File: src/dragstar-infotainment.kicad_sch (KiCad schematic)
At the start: 0 parts

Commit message: update Schematics
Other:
- note removed: "Labels are in reference to the local I/O scope boxes Labels at the cable harness are in reference to the Bus I/O Wire gauge: 1mm² / 18AWG"
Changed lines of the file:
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@@
     (date "2023-04-12")
     (rev "2.4")
-  )
-  (text "Labels are in reference to the local I/O scope boxes\nLabels at the cable harness are in reference to the Bus I/O\n\nWire gauge: 1mm² / 18AWG"
-    (at 177.8 180.34 0)
-    (effects (font (size 1.27 1.27)) (justify left bottom))
+    (comment 1 "Wire gauge: 1mm² / 18AWG")
+    (comment 3 "Labels at the cable harness are in reference to each connected component")
+    (comment 4 "Labels are in reference to the local I/O scope boxes")
   )
   (sheet (at 203.2 88.9) (size 76.2 50.8) (fields_autoplaced)

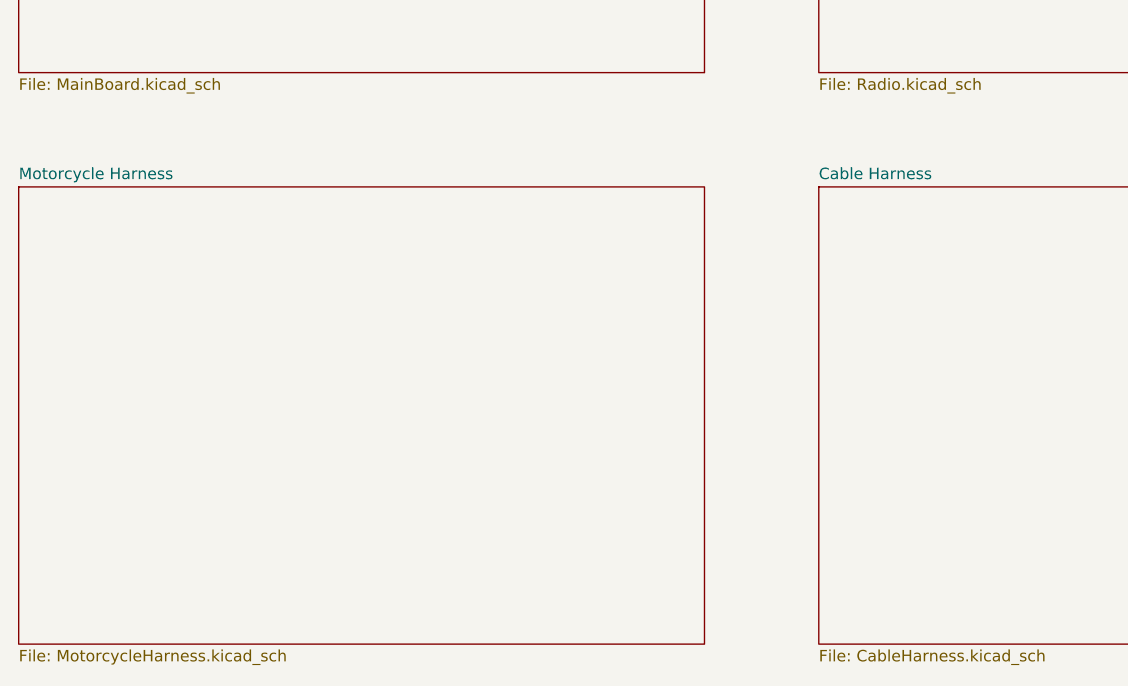
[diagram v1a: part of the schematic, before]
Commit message: simplify circuit diagram. Remove unecessary features; Split board into two components|
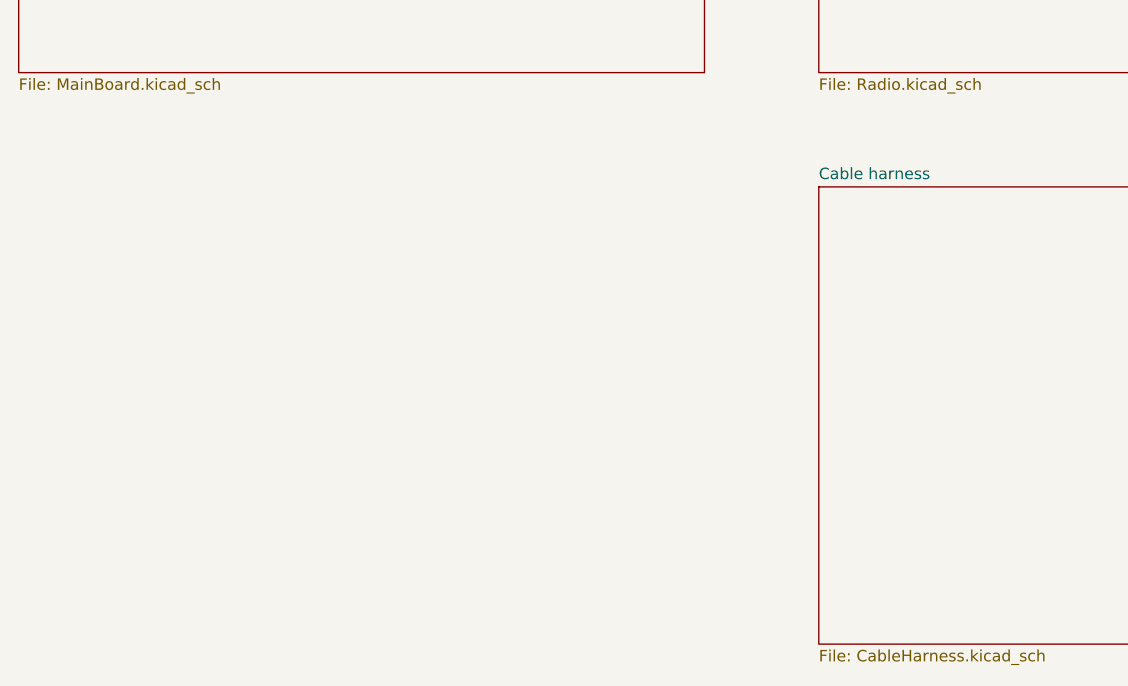
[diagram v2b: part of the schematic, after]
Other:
- sheet Cable Harness renamed Cable harness
- removed sheet Motorcycle Harness
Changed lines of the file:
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@@
     (date "2023-04-12")
     (rev "2.4")
-    (comment 1 "Wire gauge: 1mm² / 18AWG")
-    (comment 3 "Labels at the cable harness are in reference to each connected component")
-    (comment 4 "Labels are in reference to the local I/O scope boxes")
+    (comment 4 "Wire gauge: 1mm² / 18AWG")
   )
   (sheet (at 203.2 88.9) (size 76.2 50.8) (fields_autoplaced)
@@
     (stroke (width 0.1524) (type solid))
     (fill (color 0 0 0 0.0000))
-    (property "Sheetname" "Cable Harness" (at 114.3 88.1884 0)
+    (property "Sheetname" "Cable harness" (at 114.3 88.1884 0)
       (effects (font (size 1.27 1.27)) (justify left bottom))
     )
@@
       )
     )
-  )
-  (sheet (at 25.4 88.9) (size 76.2 50.8) (fields_autoplaced)
-    (stroke (width 0.1524) (type solid))
-    (fill (color 0 0 0 0.0000))
-    (property "Sheetname" "Motorcycle Harness" (at 25.4 88.1884 0)
-      (effects (font (size 1.27 1.27)) (justify left bottom))
-    )
-    (property "Sheetfile" "MotorcycleHarness.kicad_sch" (at 25.4 140.2846 0)
-      (effects (font (size 1.27 1.27)) (justify left top))
-    )
-    (instances
-      (project "dragstar-infotainment"
-        (path "/e63e39d7-6ac0-4ffd-8aa3-1841a4541b55" (page "6"))
-      )
-    )

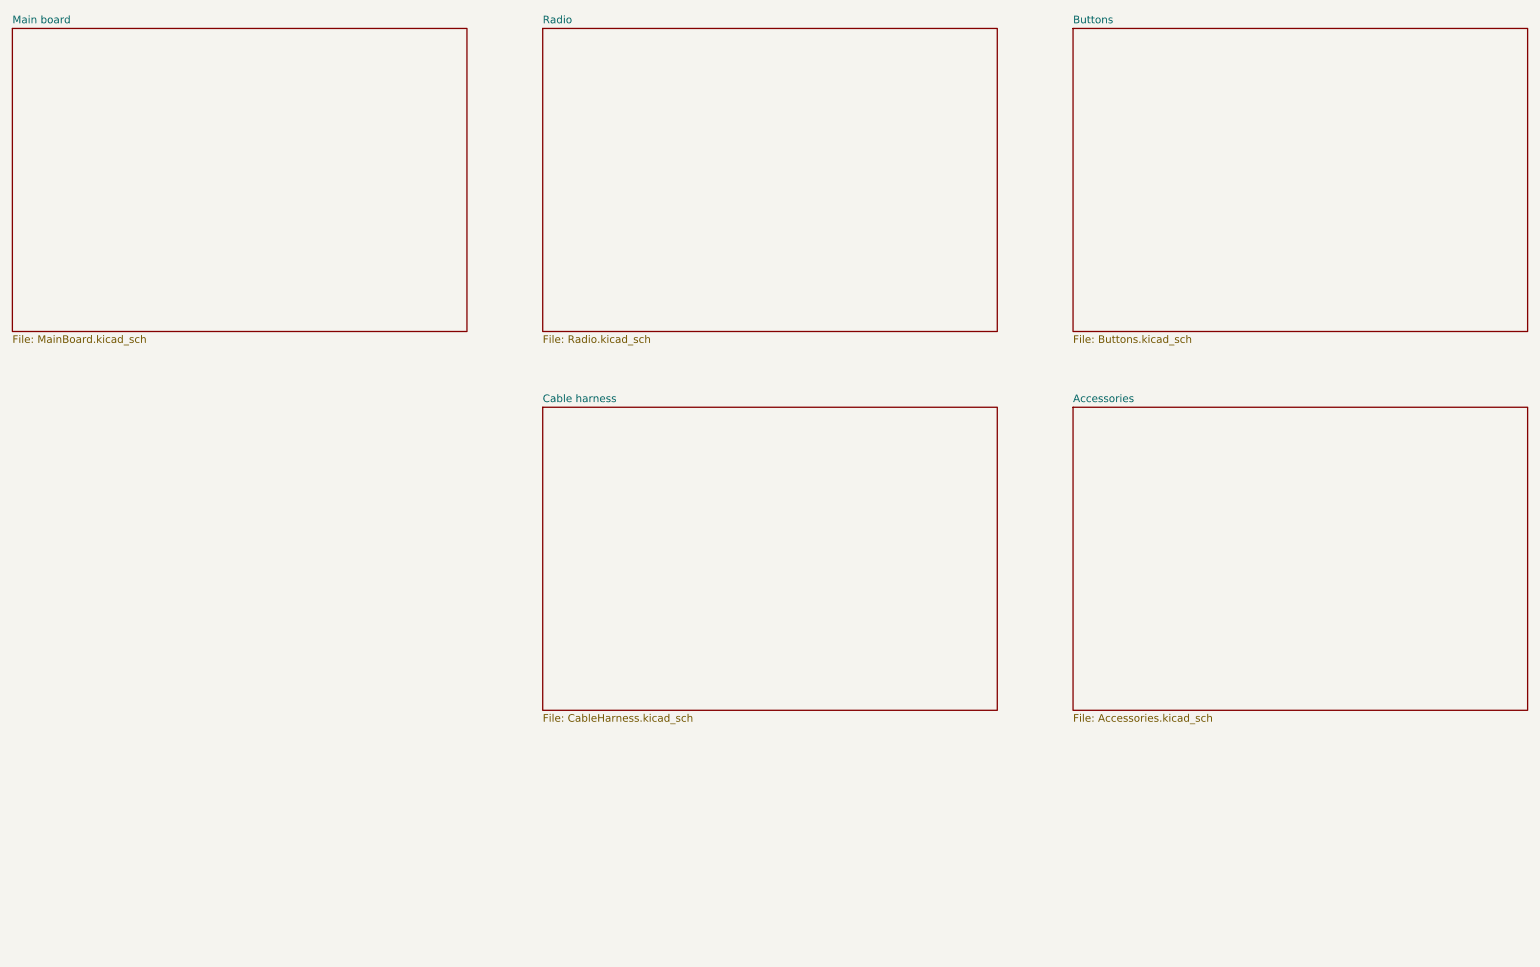
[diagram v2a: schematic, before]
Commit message: Simplify circuit diagram. Remove unecessary features
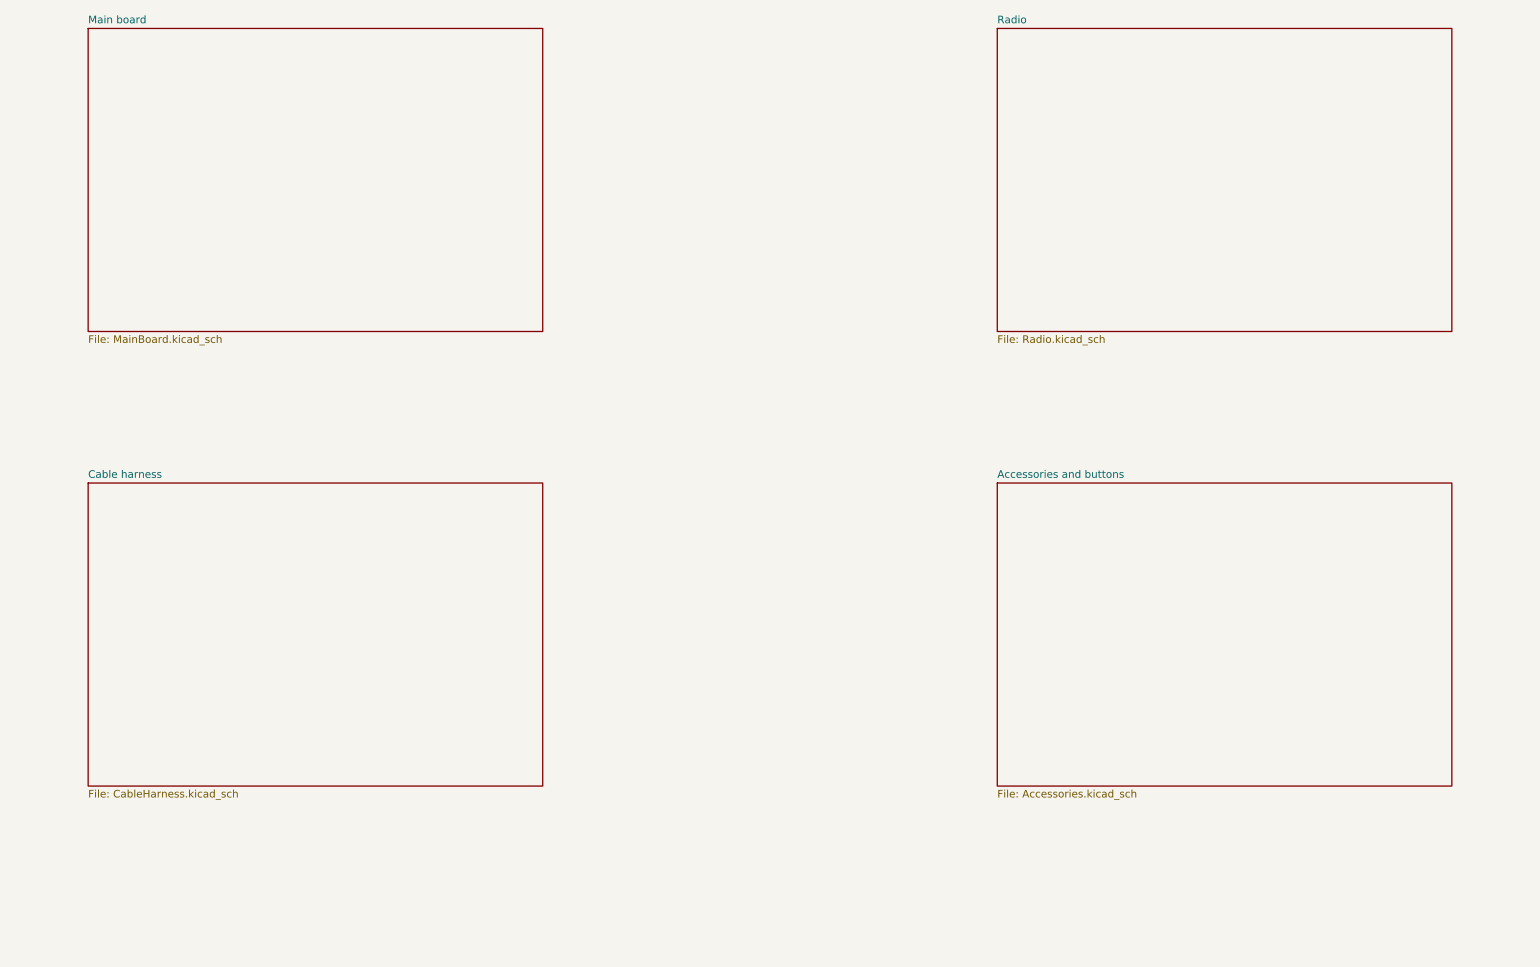
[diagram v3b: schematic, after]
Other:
- sheet Accessories renamed Accessories and buttons
- removed sheet Buttons
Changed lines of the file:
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@@
     (comment 4 "Wire gauge: 1mm² / 18AWG")
   )
-  (sheet (at 203.2 88.9) (size 76.2 50.8) (fields_autoplaced)
+  (sheet (at 190.5 101.6) (size 76.2 50.8) (fields_autoplaced)
     (stroke (width 0.1524) (type solid))
     (fill (color 0 0 0 0.0000))
-    (property "Sheetname" "Accessories" (at 203.2 88.1884 0)
+    (property "Sheetname" "Accessories and buttons" (at 190.5 100.8884 0)
       (effects (font (size 1.27 1.27)) (justify left bottom))
     )
-    (property "Sheetfile" "Accessories.kicad_sch" (at 203.2 140.2846 0)
+    (property "Sheetfile" "Accessories.kicad_sch" (at 190.5 152.9846 0)
       (effects (font (size 1.27 1.27)) (justify left top))
     )
@@
     )
   )
-  (sheet (at 25.4 25.4) (size 76.2 50.8) (fields_autoplaced)
+  (sheet (at 38.1 25.4) (size 76.2 50.8) (fields_autoplaced)
     (stroke (width 0.1524) (type solid))
     (fill (color 0 0 0 0.0000))
-    (property "Sheetname" "Main board" (at 25.4 24.6884 0)
+    (property "Sheetname" "Main board" (at 38.1 24.6884 0)
       (effects (font (size 1.27 1.27)) (justify left bottom))
     )
-    (property "Sheetfile" "MainBoard.kicad_sch" (at 25.4 76.7846 0)
+    (property "Sheetfile" "MainBoard.kicad_sch" (at 38.1 76.7846 0)
       (effects (font (size 1.27 1.27)) (justify left top))
     )
@@
     )
   )
-  (sheet (at 114.3 88.9) (size 76.2 50.8) (fields_autoplaced)
+  (sheet (at 38.1 101.6) (size 76.2 50.8) (fields_autoplaced)
     (stroke (width 0.1524) (type solid))
     (fill (color 0 0 0 0.0000))
-    (property "Sheetname" "Cable harness" (at 114.3 88.1884 0)
+    (property "Sheetname" "Cable harness" (at 38.1 100.8884 0)
       (effects (font (size 1.27 1.27)) (justify left bottom))
     )
-    (property "Sheetfile" "CableHarness.kicad_sch" (at 114.3 140.2846 0)
+    (property "Sheetfile" "CableHarness.kicad_sch" (at 38.1 152.9846 0)
       (effects (font (size 1.27 1.27)) (justify left top))
     )
@@
     )
   )
-  (sheet (at 203.2 25.4) (size 76.2 50.8) (fields_autoplaced)
+  (sheet (at 190.5 25.4) (size 76.2 50.8) (fields_autoplaced)
     (stroke (width 0.1524) (type solid))
     (fill (color 0 0 0 0.0000))
-    (property "Sheetname" "Buttons" (at 203.2 24.6884 0)
+    (property "Sheetname" "Radio" (at 190.5 24.6884 0)
       (effects (font (size 1.27 1.27)) (justify left bottom))
     )
-    (property "Sheetfile" "Buttons.kicad_sch" (at 203.2 76.7846 0)
+    (property "Sheetfile" "Radio.kicad_sch" (at 190.5 76.7846 0)
       (effects (font (size 1.27 1.27)) (justify left top))
     )
-    (instances
-      (project "dragstar-infotainment"
-        (path "/e63e39d7-6ac0-4ffd-8aa3-1841a4541b55" (page "3"))
-      )
-    )
-  )
-  (sheet (at 114.3 25.4) (size 76.2 50.8) (fields_autoplaced)
-    (stroke (width 0.1524) (type solid))
-    (fill (color 0 0 0 0.0000))
-    (property "Sheetname" "Radio" (at 114.3 24.6884 0)
-      (effects (font (size 1.27 1.27)) (justify left bottom))
-    )
-    (property "Sheetfile" "Radio.kicad_sch" (at 114.3 76.7846 0)
-      (effects (font (size 1.27 1.27)) (justify left top))
-    )
-    (property "Field2" "" (at 114.3 25.4 0)
+    (property "Field2" "" (at 190.5 25.4 0)
       (effects (font (size 1.27 1.27)) hide)
     )
